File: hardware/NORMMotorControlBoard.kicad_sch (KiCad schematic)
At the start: 2 parts, among them SW1 Reset, U1 Arduino Nano 33 BLE

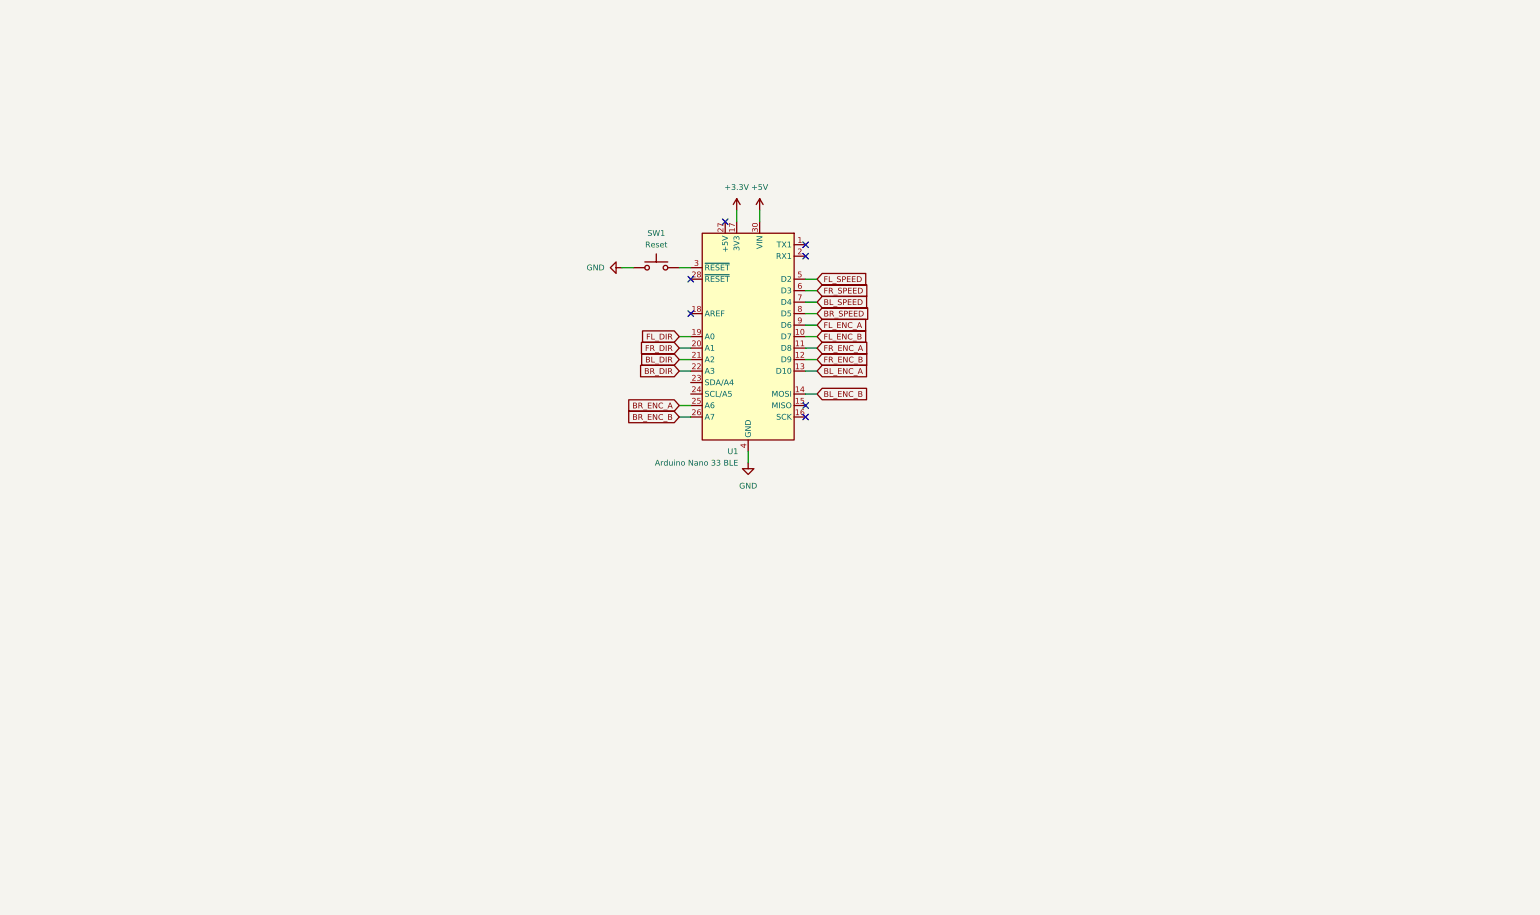
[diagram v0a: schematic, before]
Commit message: Finished schematic and placed components
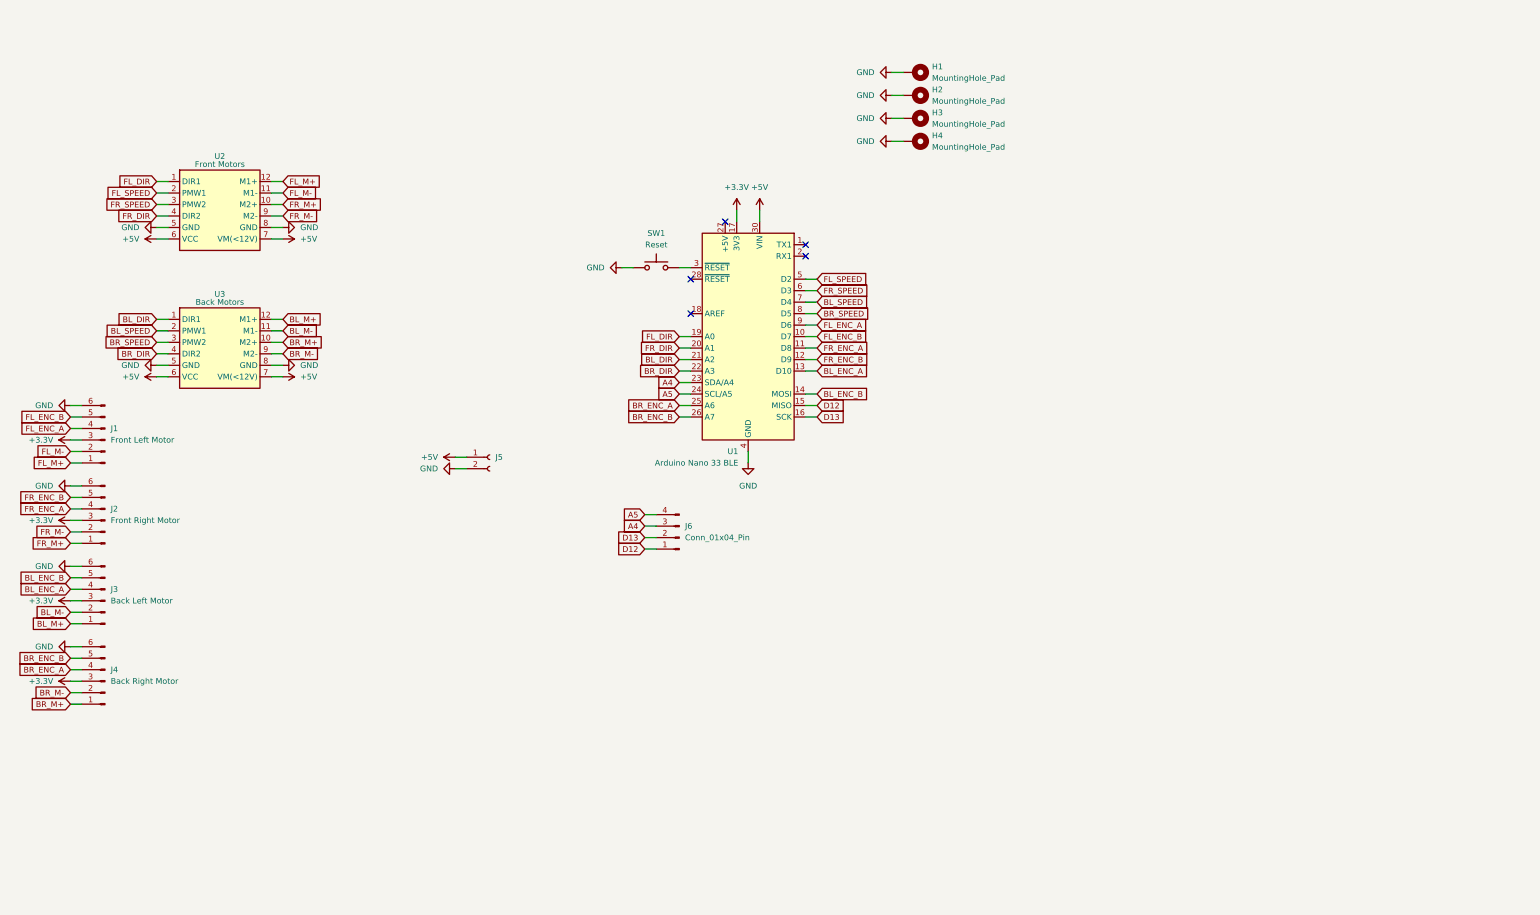
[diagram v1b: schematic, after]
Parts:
- added H1, H2, H3, H4: MountingHole_Pad, MountingHole:MountingHole_2.7mm_M2.5_Pad, symbol Mechanical:MountingHole_Pad
- added J1: Front Left Motor, Connector_PinHeader_2.54mm:PinHeader_1x06_P2.54mm_Horizontal, symbol Connector:Conn_01x06_Pin
- added J2: Front Right Motor, Connector_PinHeader_2.54mm:PinHeader_1x06_P2.54mm_Horizontal, symbol Connector:Conn_01x06_Pin
- added J3: Back Left Motor, Connector_PinHeader_2.54mm:PinHeader_1x06_P2.54mm_Horizontal, symbol Connector:Conn_01x06_Pin
- added J4: Back Right Motor, Connector_PinHeader_2.54mm:PinHeader_1x06_P2.54mm_Horizontal, symbol Connector:Conn_01x06_Pin
- added J5: Conn_01x02_Socket, Connector_Samtec_HPM_THT:Samtec_HPM-02-01-x-S_Straight_1x02_Pitch5.08mm, symbol Connector:Conn_01x02_Socket
- added J6: Conn_01x04_Pin, Connector_PinHeader_2.54mm:PinHeader_1x04_P2.54mm_Vertical, symbol Connector:Conn_01x04_Pin
- added U2: Front Motors, DFRobot_DC_Motor_Driver_Shield:DFRobot_DC_Motor_Driver_Shield, symbol DFRobot_DC_Motor_Driver_Shield:DFRobot_DC_Motor_Driver_Shield
- added U3: Back Motors, DFRobot_DC_Motor_Driver_Shield:DFRobot_DC_Motor_Driver_Shield, symbol DFRobot_DC_Motor_Driver_Shield:DFRobot_DC_Motor_Driver_Shield
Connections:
- net +3.3V: now also J1.3 (Pin_3), J2.3 (Pin_3), J3.3 (Pin_3), J4.3 (Pin_3)
- net +5V: now also J5.1 (Pin_1), U2.6 (VCC), U2.7 (VM(<12V)), U3.6 (VCC), U3.7 (VM(<12V))
- net BL_DIR: now also U3.1 (DIR1)
- net BL_ENC_A: now also J3.4 (Pin_4)
- net BL_ENC_B: now also J3.5 (Pin_5)
- net BL_SPEED: now also U3.2 (PMW1)
- net BR_DIR: now also U3.4 (DIR2)
- net BR_ENC_A: now also J4.4 (Pin_4)
- net BR_ENC_B: now also J4.5 (Pin_5)
- net BR_SPEED: now also U3.3 (PMW2)
- net FL_DIR: now also U2.1 (DIR1)
- net FL_ENC_A: now also J1.4 (Pin_4)
- net FL_ENC_B: now also J1.5 (Pin_5)
- net FL_SPEED: now also U2.2 (PMW1)
- net FR_DIR: now also U2.4 (DIR2)
- net FR_ENC_A: now also J2.4 (Pin_4)
- net FR_ENC_B: now also J2.5 (Pin_5)
- net FR_SPEED: now also U2.3 (PMW2)
- net GND: now also H1.1, H2.1, H3.1, H4.1, J1.6 (Pin_6), J2.6 (Pin_6), J3.6 (Pin_6), J4.6 (Pin_6), J5.2 (Pin_2), U2.5 (GND), U2.8 (GND), U3.5 (GND), U3.8 (GND)
- net D12: now reaches U1.15 (MISO)
- net D12: now also J6.1 (Pin_1)
- net D13: now reaches U1.16 (SCK)
- net D13: now also J6.2 (Pin_2)
- net A4: now reaches U1.23 (SDA/A4)
- net A4: now also J6.3 (Pin_3)
- net A5: now reaches U1.24 (SCL/A5)
- net A5: now also J6.4 (Pin_4)
- new net BL_M+: J3.1 (Pin_1), U3.12 (M1+)
- new net BL_M-: J3.2 (Pin_2), U3.11 (M1-)
- new net BR_M+: J4.1 (Pin_1), U3.10 (M2+)
- new net BR_M-: J4.2 (Pin_2), U3.9 (M2-)
- new net FL_M+: J1.1 (Pin_1), U2.12 (M1+)
- new net FL_M-: J1.2 (Pin_2), U2.11 (M1-)
- new net FR_M+: J2.1 (Pin_1), U2.10 (M2+)
- new net FR_M-: J2.2 (Pin_2), U2.9 (M2-)
- no-connect marks 7 -> 5

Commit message: Finished V1.0
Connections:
- net D12: now also J6.2 (Pin_2); no longer J6.1 (Pin_1)
- net D13: now also J6.1 (Pin_1); no longer J6.2 (Pin_2)

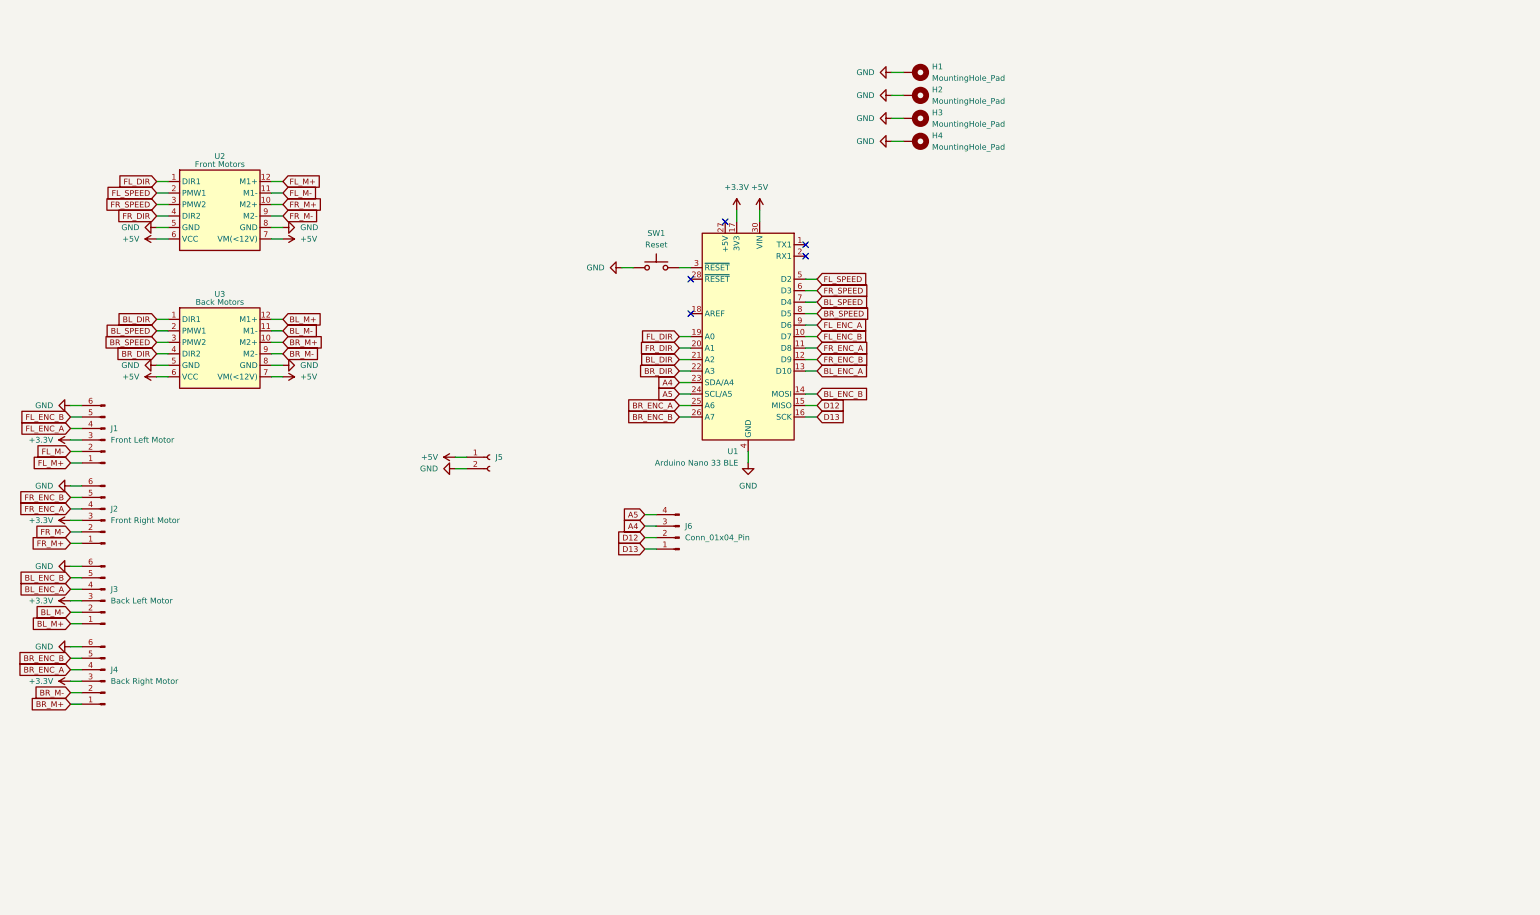
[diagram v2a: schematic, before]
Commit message: Added USB C and replaced components
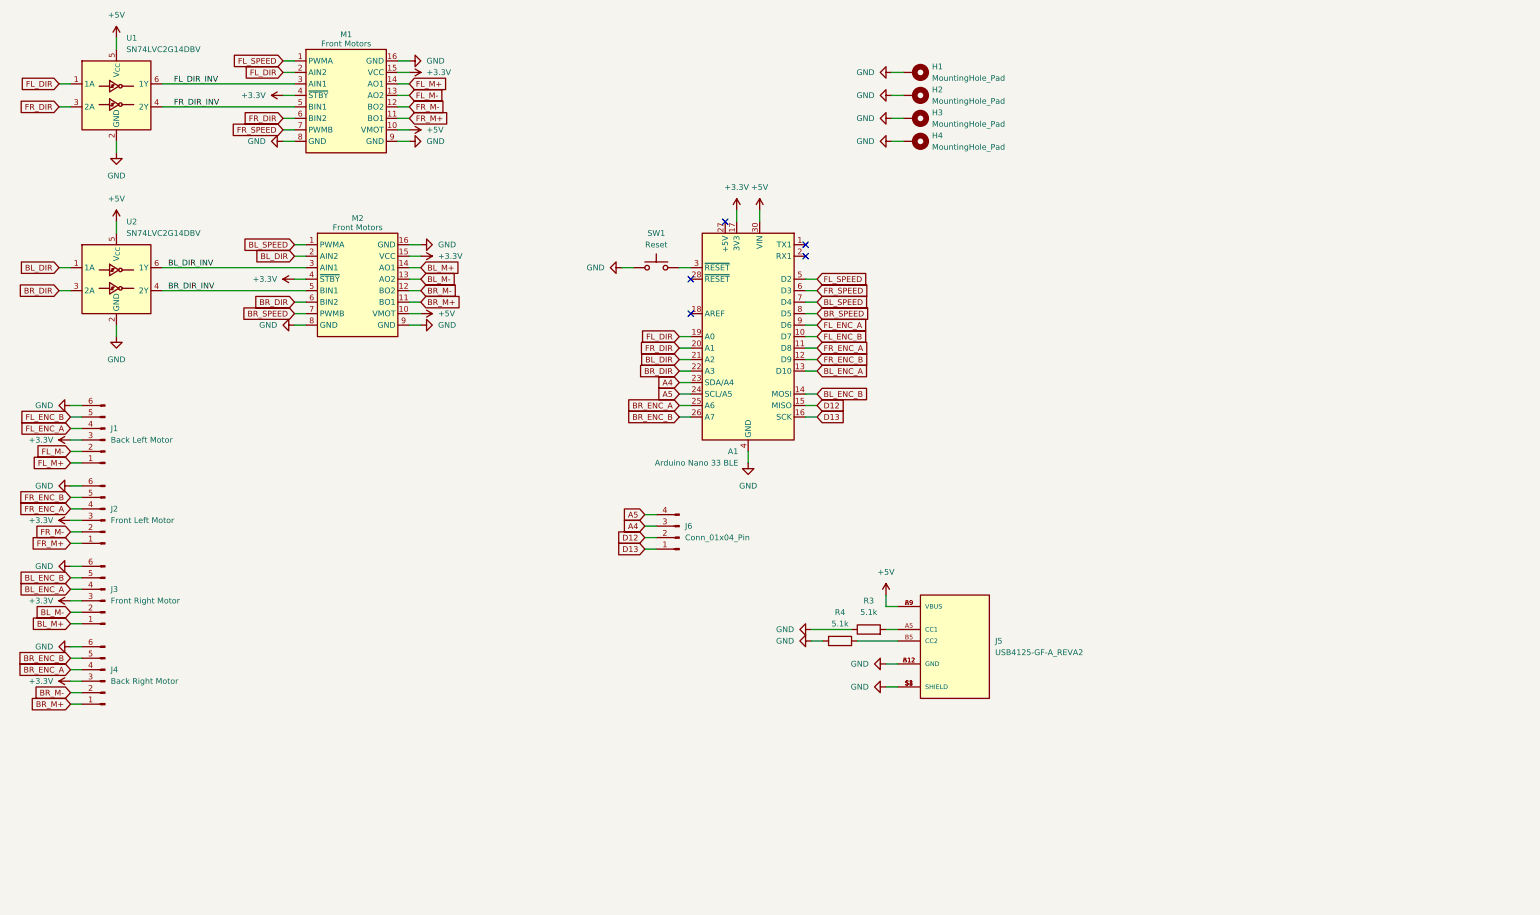
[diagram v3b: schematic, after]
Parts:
- removed J5: Conn_01x02_Socket, Connector_Samtec_HPM_THT:Samtec_HPM-02-01-x-S_Straight_1x02_Pitch5.08mm, symbol Connector:Conn_01x02_Socket
- removed U2: Front Motors, DFRobot_DC_Motor_Driver_Shield:DFRobot_DC_Motor_Driver_Shield, symbol DFRobot_DC_Motor_Driver_Shield:DFRobot_DC_Motor_Driver_Shield
- removed U3: Back Motors, DFRobot_DC_Motor_Driver_Shield:DFRobot_DC_Motor_Driver_Shield, symbol DFRobot_DC_Motor_Driver_Shield:DFRobot_DC_Motor_Driver_Shield
- added J5: USB4125-GF-A_REVA2, USB_C:USB_C, symbol USB_C:USB4125-GF-A_REVA2
- added M1, M2: Front Motors, Pololu_MD08A_Motor_Driver:Pololu_MD08A_Motor_Driver, symbol Pololu_MD08A_Motor_Driver:Pololu_MD08A_Motor_Driver
- added R3, R4: 5.1k, Resistor_SMD:R_0603_1608Metric_Pad0.98x0.95mm_HandSolder, symbol Device:R
- added U1, U2: SN74LVC2G14DBV, Package_TO_SOT_SMD:SOT-23-6, symbol 74xGxx:SN74LVC2G14DBV
- J1: value Front Left Motor -> Back Left Motor
- J2: value Front Right Motor -> Front Left Motor
- J3: value Back Left Motor -> Front Right Motor
- renumbered U1 to A1
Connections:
- net +3.3V: now also M1.15 (VCC), M1.4 (~{STBY}), M2.15 (VCC), M2.4 (~{STBY})
- net +5V: now also J5.A9 (VBUS), J5.B9 (VBUS), M1.10 (VMOT), M2.10 (VMOT), U1.5 (V_{CC}), U2.5 (V_{CC})
- net BL_DIR: now also M2.2 (AIN2), U2.1 (1A)
- net BL_M+: now also M2.14 (AO1)
- net BL_M-: now also M2.13 (AO2)
- net BL_SPEED: now also M2.1 (PWMA)
- net BR_DIR: now also M2.6 (BIN2), U2.3 (2A)
- net BR_M+: now also M2.11 (BO1)
- net BR_M-: now also M2.12 (BO2)
- net BR_SPEED: now also M2.7 (PWMB)
- net FL_DIR: now also M1.2 (AIN2), U1.1 (1A)
- net FL_M+: now also M1.14 (AO1)
- net FL_M-: now also M1.13 (AO2)
- net FL_SPEED: now also M1.1 (PWMA)
- net FR_DIR: now also M1.6 (BIN2), U1.3 (2A)
- net FR_M+: now also M1.11 (BO1)
- net FR_M-: now also M1.12 (BO2)
- net FR_SPEED: now also M1.7 (PWMB)
- net GND: now also J5.A12 (GND), J5.B12 (GND), J5.S1 (SHIELD), J5.S2 (SHIELD), J5.S3 (SHIELD), J5.S4 (SHIELD), M1.16 (GND), M1.8 (GND), M1.9 (GND), M2.16 (GND), M2.8 (GND), M2.9 (GND), R3.1, R4.1, U1.2 (GND), U2.2 (GND)
- new net: J5.B5 (CC2), R4.2
- new net: J5.A5 (CC1), R3.2
- new net BL_DIR_INV: M2.3 (AIN1), U2.6 (1Y)
- new net BR_DIR_INV: M2.5 (BIN1), U2.4 (2Y)
- new net FL_DIR_INV: M1.3 (AIN1), U1.6 (1Y)
- new net FR_DIR_INV: M1.5 (BIN1), U1.4 (2Y)

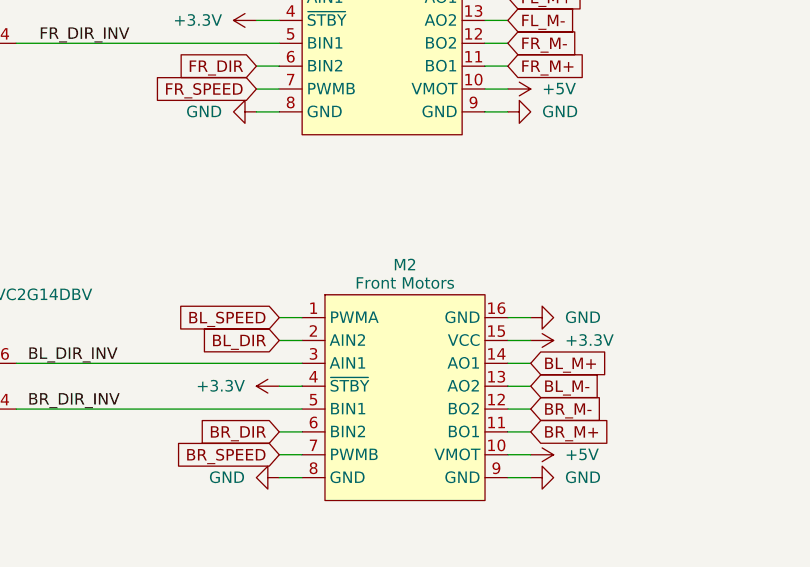
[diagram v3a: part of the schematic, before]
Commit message: renamed motor board
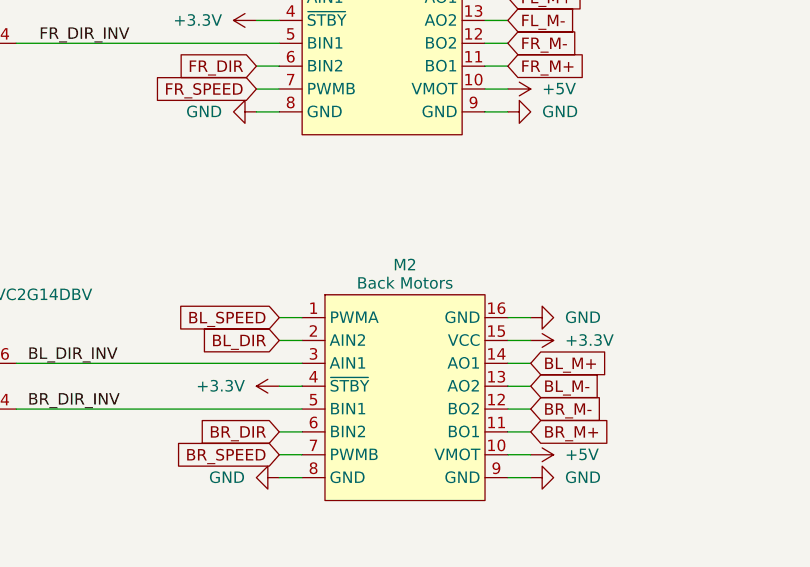
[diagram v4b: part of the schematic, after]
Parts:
- M2: value Front Motors -> Back Motors
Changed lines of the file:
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@@
 			)
 		)
-		(property "Value" "Front Motors"
+		(property "Value" "Back Motors"
 			(at 105.41 74.93 0)
 			(effects

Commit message: Exported board v1.1
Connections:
- net BL_ENC_A: now also J1.4 (Pin_4); no longer J3.4 (Pin_4)
- net BL_ENC_B: now also J1.5 (Pin_5); no longer J3.5 (Pin_5)
- net BL_M+: now also J1.1 (Pin_1); no longer J3.1 (Pin_1)
- net BL_M-: now also J1.2 (Pin_2); no longer J3.2 (Pin_2)
- net FL_ENC_A: now also J2.4 (Pin_4); no longer J1.4 (Pin_4)
- net FL_ENC_B: now also J2.5 (Pin_5); no longer J1.5 (Pin_5)
- net FL_M+: now also J2.1 (Pin_1); no longer J1.1 (Pin_1)
- net FL_M-: now also J2.2 (Pin_2); no longer J1.2 (Pin_2)
- net FR_ENC_A: now also J3.4 (Pin_4); no longer J2.4 (Pin_4)
- net FR_ENC_B: now also J3.5 (Pin_5); no longer J2.5 (Pin_5)
- net FR_M+: now also J3.1 (Pin_1); no longer J2.1 (Pin_1)
- net FR_M-: now also J3.2 (Pin_2); no longer J2.2 (Pin_2)
